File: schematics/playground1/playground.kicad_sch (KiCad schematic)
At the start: 35 parts, among them SW1 SW_SPST, U1 ADS1299, U2 TLV75533PDBV, U3 AP2112K-5.0

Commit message: IP - work on integrating pic32
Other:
- added sheet pic32 (pic32.kicad_sch)
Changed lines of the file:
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@@
+		)
+	)
+	(sheet
+		(at 0.254 225.806)
+		(size 35.306 31.496)
+		(exclude_from_sim no)
+		(in_bom yes)
+		(on_board yes)
+		(dnp no)
+		(fields_autoplaced yes)
+		(stroke
+			(width 0.1524)
+			(type solid)
+		)
+		(fill
+			(color 0 0 0 0.0000)
+		)
+		(property "Sheetname" "pic32"
+			(at 0.254 225.0944 0)
+			(effects
+				(font
+					(size 1.27 1.27)
+				)
+				(justify left bottom)
+			)
+		)
+		(property "Sheetfile" "pic32.kicad_sch"
+			(at 0.254 257.8866 0)
+			(effects
+				(font
+					(size 1.27 1.27)
+				)
+				(justify left top)
+			)
+		)
+		(instances
+			(project "playground"
+				(path "/238de170-6a90-40ad-afaf-ab931b754487"
+					(page "2")
+				)
+			)
 		)
 	)

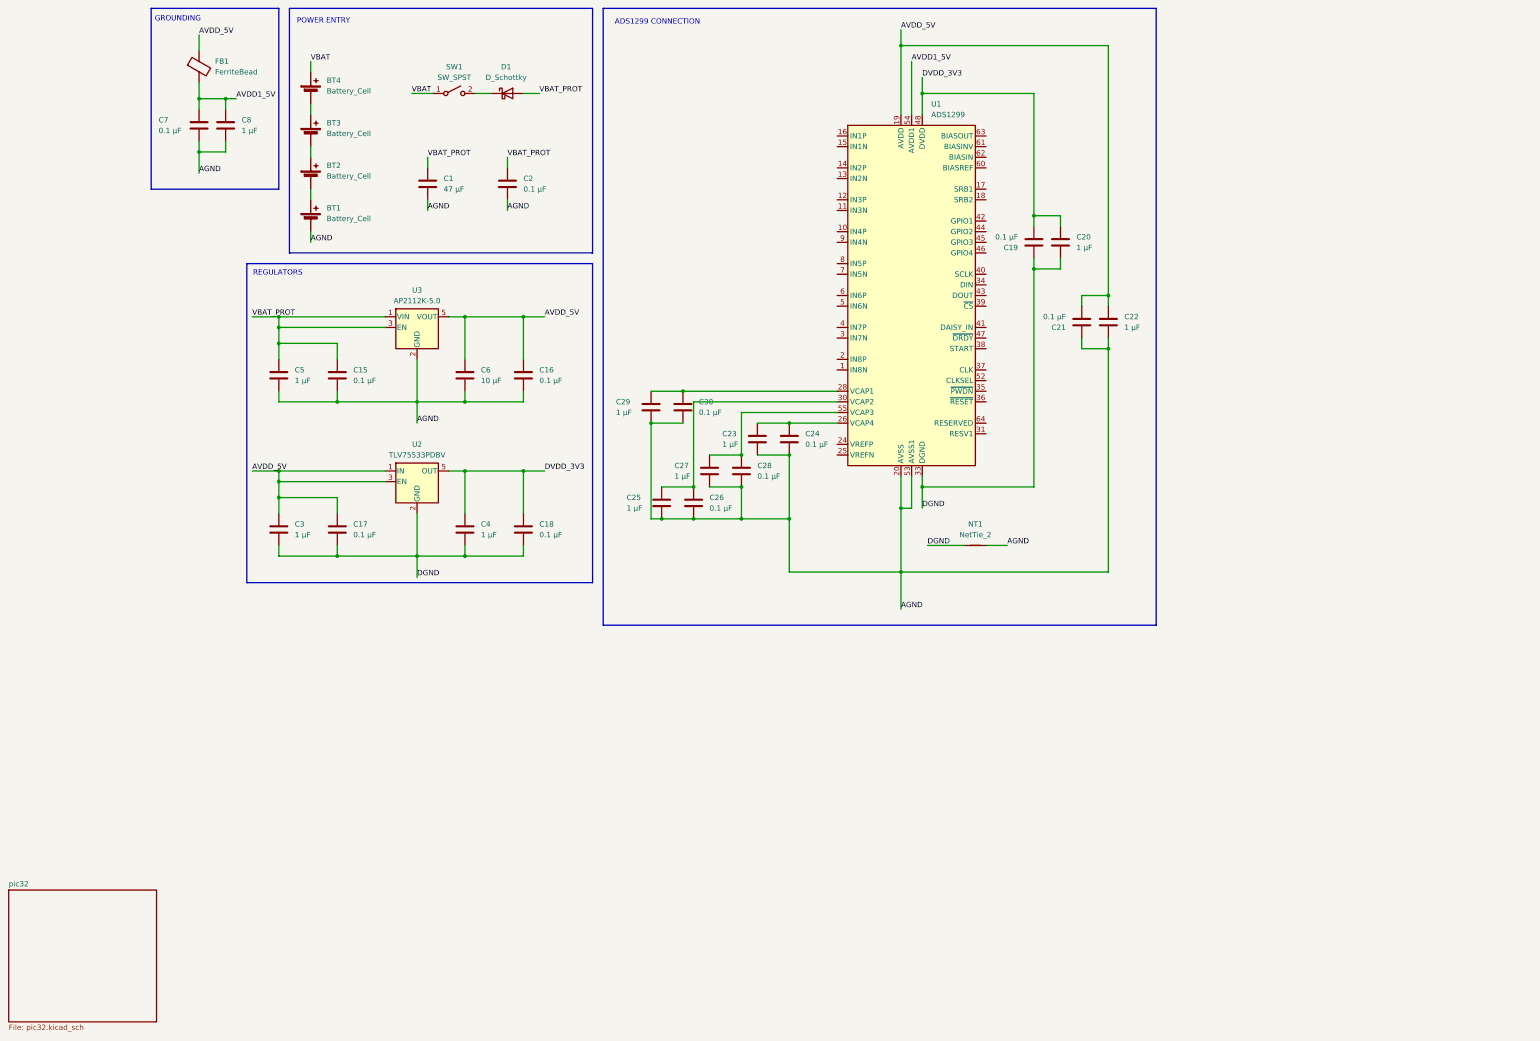
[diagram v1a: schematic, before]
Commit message: channel input protection
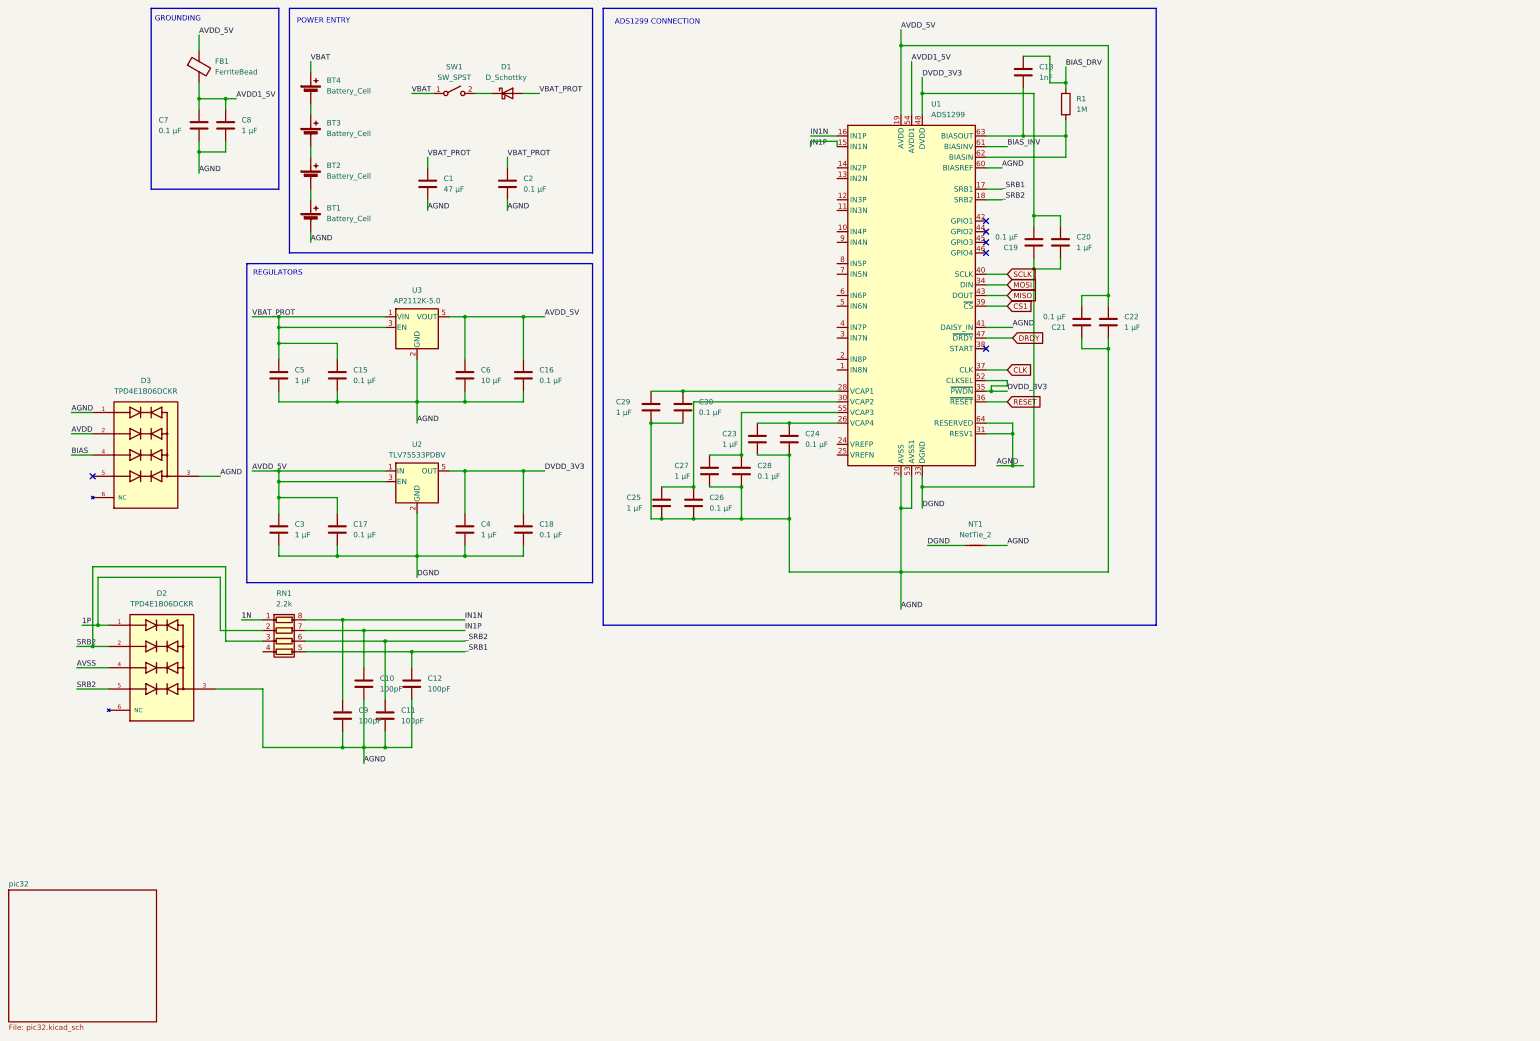
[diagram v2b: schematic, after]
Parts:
- added C10, C11, C12, C9: 100pF, symbol Device:C
- added C13: 1nF, symbol Device:C
- added D2, D3: TPD4E1B06DCKR, TPD4E1B06DCKR:TVS_TPD4E1B06DCKR, symbol TPD4E1B06DCKR:TPD4E1B06DCKR
- added R1: 1M, symbol Device:R
- added RN1: 2.2k, symbol Device:R_Pack04
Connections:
- net AGND: now also U1.31 (RESV1), U1.41 (DAISY_IN), U1.60 (BIASREF), U1.64 (RESERVED), C10.2, C11.2, C12.2, C9.2, D2.3, D3.1, D3.3
- net DVDD_3V3: now also U1.35 (~{PWDN}), U1.52 (CLKSEL)
- net IN1P: now reaches U1.15 (IN1N)
- net IN1P: now also C10.1, RN1.7 (R2.2)
- net IN1N: now reaches U1.16 (IN1P)
- net IN1N: now also C9.1, RN1.8 (R1.2)
- net _SRB1: now reaches U1.17 (SRB1)
- net _SRB1: now also C12.1, RN1.5 (R4.2)
- net _SRB2: now reaches U1.18 (SRB2)
- net _SRB2: now also C11.1, RN1.6 (R3.2)
- net MOSI: now reaches U1.34 (DIN)
- net RESET: now reaches U1.36 (~{RESET})
- net CLK: now reaches U1.37 (CLK)
- net CS1: now reaches U1.39 (~{CS})
- net SCLK: now reaches U1.40 (SCLK)
- net MISO: now reaches U1.43 (DOUT)
- net DRDY: now reaches U1.47 (~{DRDY})
- net BIAS_INV: now reaches U1.61 (BIASINV)
- net at U1.62 (BIASIN): now also U1.63 (BIASOUT), C13.2, R1.2
- new net 1N: RN1.1 (R1.1)
- new net 1P: D2.1, RN1.2 (R2.1)
- new net AVDD: D3.2
- new net AVSS: D2.4
- new net BIAS: D3.4
- new net BIAS_DRV: C13.1, R1.1
- new net SRB2: D2.2, D2.5, RN1.3 (R3.1)
- no-connect marks 0 -> 6

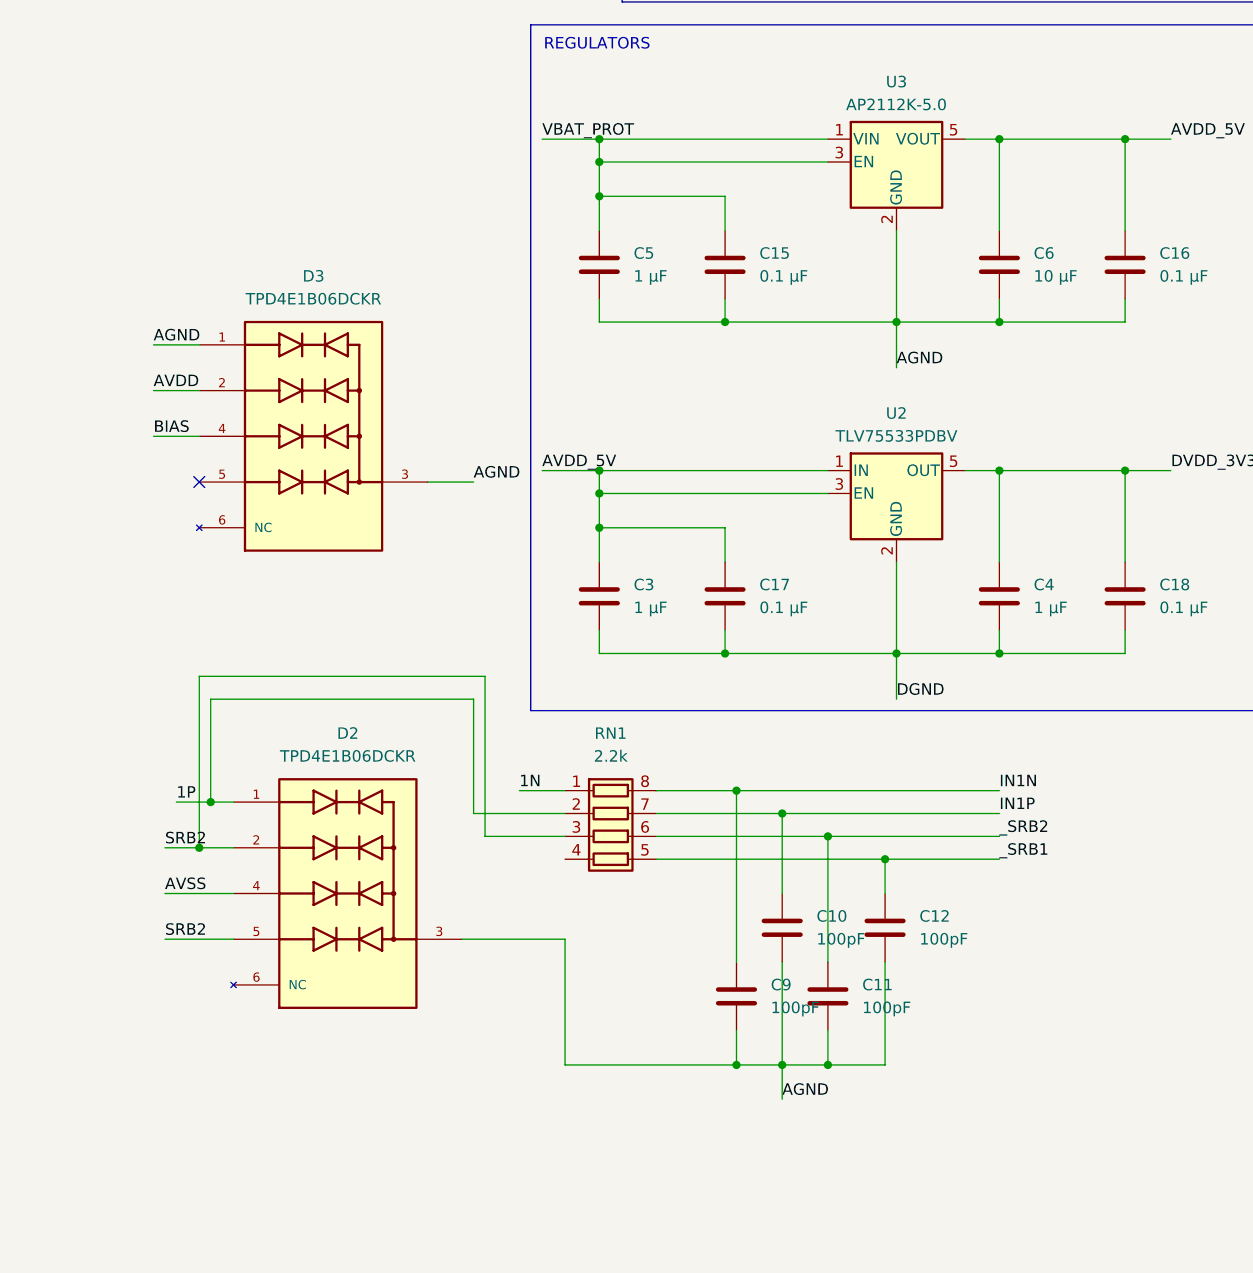
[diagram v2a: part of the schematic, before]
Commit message: channel input protection + bias/power protection
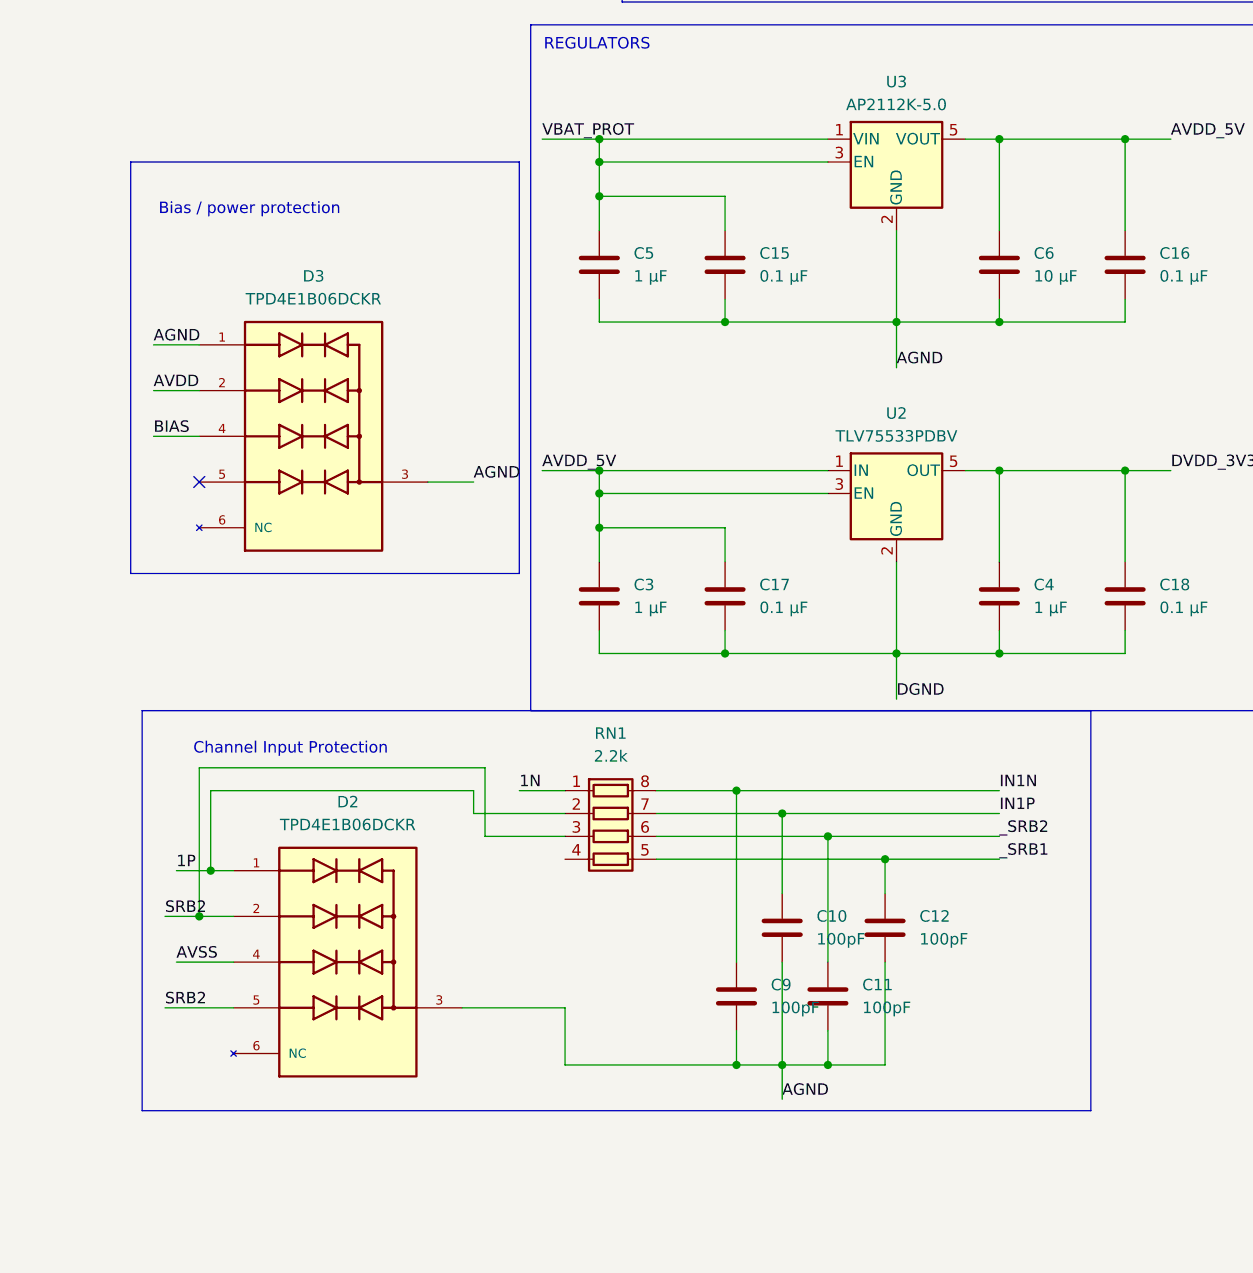
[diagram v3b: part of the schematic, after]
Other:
- note added: "Bias / power protection"
- note added: "Channel Input Protection"
- moved on the sheet: D2
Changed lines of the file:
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@@
 	)
 	(rectangle
+		(start 13.97 152.4)
+		(end 119.38 196.85)
+		(stroke
+			(width 0)
+			(type default)
+		)
+		(fill
+			(type none)
+		)
+	)
+	(rectangle
 		(start 67.31 15.24)
 		(end 139.7 73.66)
@@
 		)
 	)
+	(rectangle
+		(start 12.7 91.44)
+		(end 55.88 137.16)
+		(stroke
+			(width 0)
+			(type default)
+		)
+		(fill
+			(type none)
+		)
+	)
+	(text "Channel Input Protection"
+		(exclude_from_sim no)
+		(at 30.48 156.718 0)
+		(effects
+			(font
+				(size 1.27 1.27)
+			)
+		)
+	)
 	(text "POWER ENTRY"
 		(exclude_from_sim no)
@@
 		)
 	)
+	(text "Bias / power protection"
+		(exclude_from_sim no)
+		(at 25.908 96.774 0)
+		(effects
+			(font
+				(size 1.27 1.27)
+			)
+		)
+	)
 	(text "GROUNDING"
 		(exclude_from_sim no)
@@
 	)
 	(junction
+		(at 21.59 170.18)
+		(diameter 0)
+		(color 0 0 0 0)
+	)
+	(junction
 		(at 52.07 36.83)
 		(diameter 0)
@@
 	)
 	(junction
-		(at 21.59 162.56)
-		(diameter 0)
-		(color 0 0 0 0)
-	)
-	(junction
 		(at 80.01 191.77)
 		(diameter 0)
@@
 	)
 	(junction
-		(at 20.32 167.64)
+		(at 213.36 149.86)
 		(diameter 0)
 		(color 0 0 0 0)
 	)
 	(junction
-		(at 213.36 149.86)
+		(at 163.83 129.54)
 		(diameter 0)
 		(color 0 0 0 0)
 	)
 	(junction
-		(at 163.83 129.54)
+		(at 153.67 114.3)
 		(diameter 0)
 		(color 0 0 0 0)
 	)
 	(junction
-		(at 153.67 114.3)
+		(at 20.32 175.26)
 		(diameter 0)
 		(color 0 0 0 0)
@@
 	(wire
 		(pts
+			(xy 21.59 161.29) (xy 21.59 170.18)
+		)
+		(stroke
+			(width 0)
+			(type default)
+		)
+	)
+	(wire
+		(pts
 			(xy 234.95 106.68) (xy 238.76 106.68)
 		)
@@
 	(wire
 		(pts
+			(xy 17.78 180.34) (xy 24.13 180.34)
+		)
+		(stroke
+			(width 0)
+			(type default)
+		)
+	)
+	(wire
+		(pts
 			(xy 233.68 78.74) (xy 238.76 78.74)
 		)
@@
 	(wire
 		(pts
-			(xy 49.53 177.8) (xy 60.96 177.8)
+			(xy 49.53 185.42) (xy 60.96 185.42)
 		)
 		(stroke
@@
 	(wire
 		(pts
-			(xy 16.51 172.72) (xy 24.13 172.72)
+			(xy 16.51 185.42) (xy 24.13 185.42)
 		)
 		(stroke
@@
 	(wire
 		(pts
-			(xy 20.32 167.64) (xy 24.13 167.64)
+			(xy 20.32 175.26) (xy 24.13 175.26)
 		)
 		(stroke
@@
 	(wire
 		(pts
-			(xy 20.32 148.59) (xy 52.07 148.59)
+			(xy 20.32 158.75) (xy 52.07 158.75)
 		)
 		(stroke
@@
 	(wire
 		(pts
-			(xy 21.59 151.13) (xy 50.8 151.13)
+			(xy 21.59 161.29) (xy 50.8 161.29)
 		)
 		(stroke
@@
 	(wire
 		(pts
-			(xy 52.07 148.59) (xy 52.07 166.37)
+			(xy 52.07 158.75) (xy 52.07 166.37)
 		)
 		(stroke
@@
 	(wire
 		(pts
-			(xy 20.32 167.64) (xy 20.32 148.59)
+			(xy 20.32 158.75) (xy 20.32 175.26)
 		)
 		(stroke
@@
 	(wire
 		(pts
-			(xy 16.51 177.8) (xy 24.13 177.8)
-		)
-		(stroke
-			(width 0)
-			(type default)
-		)
-	)
-	(wire
-		(pts
 			(xy 100.33 50.8) (xy 100.33 53.34)
 		)
@@
 	(wire
 		(pts
-			(xy 16.51 167.64) (xy 20.32 167.64)
+			(xy 16.51 175.26) (xy 20.32 175.26)
 		)
 		(stroke
@@
 	(wire
 		(pts
-			(xy 21.59 162.56) (xy 21.59 151.13)
-		)
-		(stroke
-			(width 0)
-			(type default)
-		)
-	)
-	(wire
-		(pts
 			(xy 71.12 163.83) (xy 85.09 163.83)
 		)
@@
 	(wire
 		(pts
-			(xy 17.78 162.56) (xy 21.59 162.56)
+			(xy 17.78 170.18) (xy 21.59 170.18)
 		)
 		(stroke
@@
 	(wire
 		(pts
-			(xy 50.8 151.13) (xy 50.8 163.83)
+			(xy 50.8 161.29) (xy 50.8 163.83)
 		)
 		(stroke
@@
 	(wire
 		(pts
-			(xy 21.59 162.56) (xy 24.13 162.56)
+			(xy 21.59 170.18) (xy 24.13 170.18)
 		)
 		(stroke
@@
 	(wire
 		(pts
-			(xy 60.96 177.8) (xy 60.96 191.77)
+			(xy 60.96 185.42) (xy 60.96 191.77)
 		)
 		(stroke
@@
 	)
 	(label "SRB2"
-		(at 16.51 167.64 0)
+		(at 16.51 175.26 0)
 		(effects
 			(font
@@
 	)
 	(label "SRB2"
-		(at 16.51 177.8 0)
+		(at 16.51 185.42 0)
 		(effects
 			(font
@@
 	)
 	(label "1P"
-		(at 17.78 162.56 0)
+		(at 17.78 170.18 0)
 		(effects
 			(font
@@
 	)
 	(label "AVSS"
-		(at 16.51 172.72 0)
+		(at 17.78 180.34 0)
 		(effects
 			(font
@@
 	(symbol
 		(lib_id "TPD4E1B06DCKR:TPD4E1B06DCKR")
-		(at 36.83 172.72 0)
+		(at 36.83 180.34 0)
 		(unit 1)
 		(exclude_from_sim no)
@@
 		(fields_autoplaced yes)
 		(property "Reference" "D2"
-			(at 36.83 154.94 0)
+			(at 36.83 162.56 0)
 			(effects
 				(font
@@
 		)
 		(property "Value" "TPD4E1B06DCKR"
-			(at 36.83 157.48 0)
+			(at 36.83 165.1 0)
 			(effects
 				(font
@@
 		)
 		(property "Footprint" "TPD4E1B06DCKR:TVS_TPD4E1B06DCKR"
-			(at 36.83 172.72 0)
+			(at 36.83 180.34 0)
 			(effects
 				(font
@@
 		)
 		(property "Datasheet" ""
-			(at 36.83 172.72 0)
+			(at 36.83 180.34 0)
 			(effects
 				(font
@@
 		)
 		(property "Description" ""
-			(at 36.83 172.72 0)
+			(at 36.83 180.34 0)
 			(effects
 				(font
@@
 		)
 		(property "MF" "Texas Instruments"
-			(at 36.83 172.72 0)
+			(at 36.83 180.34 0)
 			(effects
 				(font
@@
 		)
 		(property "MAXIMUM_PACKAGE_HEIGHT" "1.1 mm"
-			(at 36.83 172.72 0)
+			(at 36.83 180.34 0)
 			(effects
 				(font
@@
 		)
 		(property "Package" "SOT-SC70-6 Texas Instruments"
-			(at 36.83 172.72 0)
+			(at 36.83 180.34 0)
 			(effects
 				(font
@@
 		)
 		(property "Price" "None"
-			(at 36.83 172.72 0)
+			(at 36.83 180.34 0)
 			(effects
 				(font
@@
 		)
 		(property "Check_prices" "https://www.snapeda.com/parts/TPD4E1B06DCKR/Texas+Instruments/view-part/?ref=eda"
-			(at 36.83 172.72 0)
+			(at 36.83 180.34 0)
 			(effects
 				(font
@@
 		)
 		(property "STANDARD" "Manufacturer Recommendations"
-			(at 36.83 172.72 0)
+			(at 36.83 180.34 0)
 			(effects
 				(font
@@
 		)
 		(property "PARTREV" "C"
-			(at 36.83 172.72 0)
+			(at 36.83 180.34 0)
 			(effects
 				(font
@@
 		)
 		(property "SnapEDA_Link" "https://www.snapeda.com/parts/TPD4E1B06DCKR/Texas+Instruments/view-part/?ref=snap"
-			(at 36.83 172.72 0)
+			(at 36.83 180.34 0)
 			(effects
 				(font
@@
 		)
 		(property "MP" "TPD4E1B06DCKR"
-			(at 36.83 172.72 0)
+			(at 36.83 180.34 0)
 			(effects
 				(font
@@
 		)
 		(property "Purchase-URL" "https://www.snapeda.com/api/url_track_click_mouser/?unipart_id=46121&manufacturer=Texas Instruments&part_name=TPD4E1B06DCKR&search_term=None"
-			(at 36.83 172.72 0)
+			(at 36.83 180.34 0)
 			(effects
 				(font
@@
 		)
 		(property "Description_1" "Quad 0.7-pF, ±5.5-V, ±12-kV ESD protection diode with 0.5-nA max leakage in SOT & SC70 packages"
-			(at 36.83 172.72 0)
+			(at 36.83 180.34 0)
 			(effects
 				(font
@@
 		)
 		(property "MANUFACTURER" "Texas Instruments"
-			(at 36.83 172.72 0)
+			(at 36.83 180.34 0)
 			(effects
 				(font
@@
 		)
 		(property "Availability" "In Stock"
-			(at 36.83 172.72 0)
+			(at 36.83 180.34 0)
 			(effects
 				(font
@@
 		)
 		(property "SNAPEDA_PN" "TPD4E1B06DCKR"
-			(at 36.83 172.72 0)
+			(at 36.83 180.34 0)
 			(effects
 				(font
